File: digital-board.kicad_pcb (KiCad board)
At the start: 2 copper layers, 200 x 150 mm, 233 parts, among them IC1 ATMEGA6450-A, J1 CONN_20X2, Q1 2N3904, Q2 2N3904, SW15 TACT_SWITCH, SW16 TACT_SWITCH, SW17 TACT_SWITCH, SW18 TACT_SWITCH, SW19 TACT_SWITCH, SW20 TACT_SWITCH, SW21 TACT_SWITCH, SW22 TACT_SWITCH, SW23 TACT_SWITCH, U1 DG419, U10 74LVC1G32, U11 74HC165, U12 74AC595, U13 74AC595, U14 74HC165, U15 74AC595, U16 74AC595, U2 74HC4067, U3 R-78E5.0-1.0, U4 74HC4067, U5 74LS573, U6 74LS573, U7 74LVC2G04, U8 74AC595, U9 74HC165, X1 MIDI OUT, X2 MIDI IN, X3 MIDI THRU

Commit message: routing
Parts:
- removed C18: 0.1µ, synth:SM0603-JRL
- removed U11: 74HC165, github-smd:TSSOP-16
- moved R53 69.2 mm to (46.0, 51.0)
- moved C9 4.53 mm to (131.0, 72.0), turned to 270 degrees
- moved C17 3.04 mm to (187.0, 113.5), turned to 270 degrees
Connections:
- IC1 pad 86: Net-(IC1-Pad86) -> ~POTMUX EN0
- IC1 pad 87: Net-(IC1-Pad87) -> ~POTMUX EN1
- IC1 pad 90: ~POTMUX EN1 -> ISW10
- IC1 pad 91: ~POTMUX EN0 -> SW21
- IC1 pad 92: DGATE -> SW22
- IC1 pad 93: Net-(IC1-Pad93) -> ISW11
- IC1 pad 94: Net-(IC1-Pad94) -> ISW9
- IC1 pad 95: Net-(IC1-Pad95) -> ISW8
- IC1 pad 96: Net-(IC1-Pad96) -> DGATE
- ISW10 pad 2: Net-(ISW10-Pad2) -> ISW10
- ISW11 pad 2: Net-(ISW11-Pad2) -> ISW11
- ISW8 pad 2: Net-(ISW8-Pad2) -> ISW8
- ISW9 pad 2: Net-(ISW9-Pad2) -> ISW9
- R37 pad 2: Net-(ISW9-Pad2) -> ISW9
- R41 pad 2: Net-(ISW8-Pad2) -> ISW8
- R45 pad 2: Net-(R45-Pad2) -> SW21
- R51 pad 2: Net-(R51-Pad2) -> SW22
- R56 pad 2: Net-(ISW11-Pad2) -> ISW11
- R60 pad 2: Net-(ISW10-Pad2) -> ISW10
- SW21 pad 2: Net-(R45-Pad2) -> SW21
- SW22 pad 2: Net-(R51-Pad2) -> SW22
- U14 pad 15: GND -> ~SPI_EN
- U14 pad 9: Net-(U11-Pad10) -> SPI_MISO
- VR16 pad 2: Net-(U4-Pad6) -> Net-(U4-Pad8)
- VR17 pad 2: Net-(U4-Pad7) -> Net-(U4-Pad6)
- VR18 pad 2: Net-(U4-Pad8) -> Net-(U4-Pad7)
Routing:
- net ISW9: track 0.00 -> 140.6 mm, vias 0 -> 1
- net GND: track 3.57 -> 123.3 mm
- net DGATE: track 0.00 -> 104.0 mm, vias 0 -> 1
- net ISW8: track 0.00 -> 83.0 mm, vias 0 -> 1
- net ISW10: track 0.00 -> 82.7 mm, vias 0 -> 1
- net Net-(U4-Pad6): track 0.00 -> 77.0 mm
- net ISW11: track 0.00 -> 71.3 mm, vias 0 -> 1
- net SW22: track 0.00 -> 51.6 mm, vias 0 -> 1
- net SW21: track 0.00 -> 31.5 mm, vias 0 -> 1
- net Net-(ISW8-Pad2): track 26.8 -> 0.00 mm
- net Net-(U4-Pad7): track 76.5 -> 53.9 mm
- net Net-(U4-Pad8): track 53.3 -> 35.0 mm
- net Net-(ISW9-Pad2): track 11.3 -> 0.00 mm
- net Net-(R51-Pad2): track 10.8 -> 0.00 mm
- net Net-(R45-Pad2): track 10.8 -> 0.00 mm
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
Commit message: just before first ses import
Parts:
- R1: moved to F.Cu
- moved LED1 18.7 mm to (103.5, 164.0)
- moved R4 18.7 mm to (103.5, 162.0)
- moved R1 4.03 mm to (100.0, 140.5), turned to 0 degrees
- moved C5 4.00 mm to (114.0, 145.5), turned to 0 degrees
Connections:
- R4 pad 2: Net-(IC1-Pad4) -> Net-(R4-Pad2)
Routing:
- net +5V: track 347.2 -> 597.0 mm, vias 2 -> 1
- net UART TX: track 0.00 -> 245.5 mm
- net TUNE SEL: track 0.00 -> 167.4 mm, vias 0 -> 2
- net GATE: track 15.4 -> 130.7 mm, vias 0 -> 1
- net DISP CATHODE LATCH: track 0.00 -> 35.8 mm, vias 0 -> 2
- net DISP ANODE LATCH: track 0.00 -> 32.5 mm, vias 0 -> 2
- net ~RESET: track 17.9 -> 34.6 mm, vias 0 -> 1
- net Net-(IC1-Pad4): track 4.20 -> 0.00 mm
- net Net-(C3-Pad2): track 12.4 -> 15.9 mm
- net MISO: track 28.0 -> 31.3 mm
- net Net-(ISW11-Pad6): track 0.00 -> 2.95 mm
- net ISW10: track 82.7 -> 80.2 mm
- net Net-(LED1-Pad1): track 2.08 -> 0.00 mm
- net Net-(C5-Pad1): track 5.10 -> 6.79 mm
- net Net-(R42-Pad2): track 0.00 -> 1.63 mm, vias 0 -> 1
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
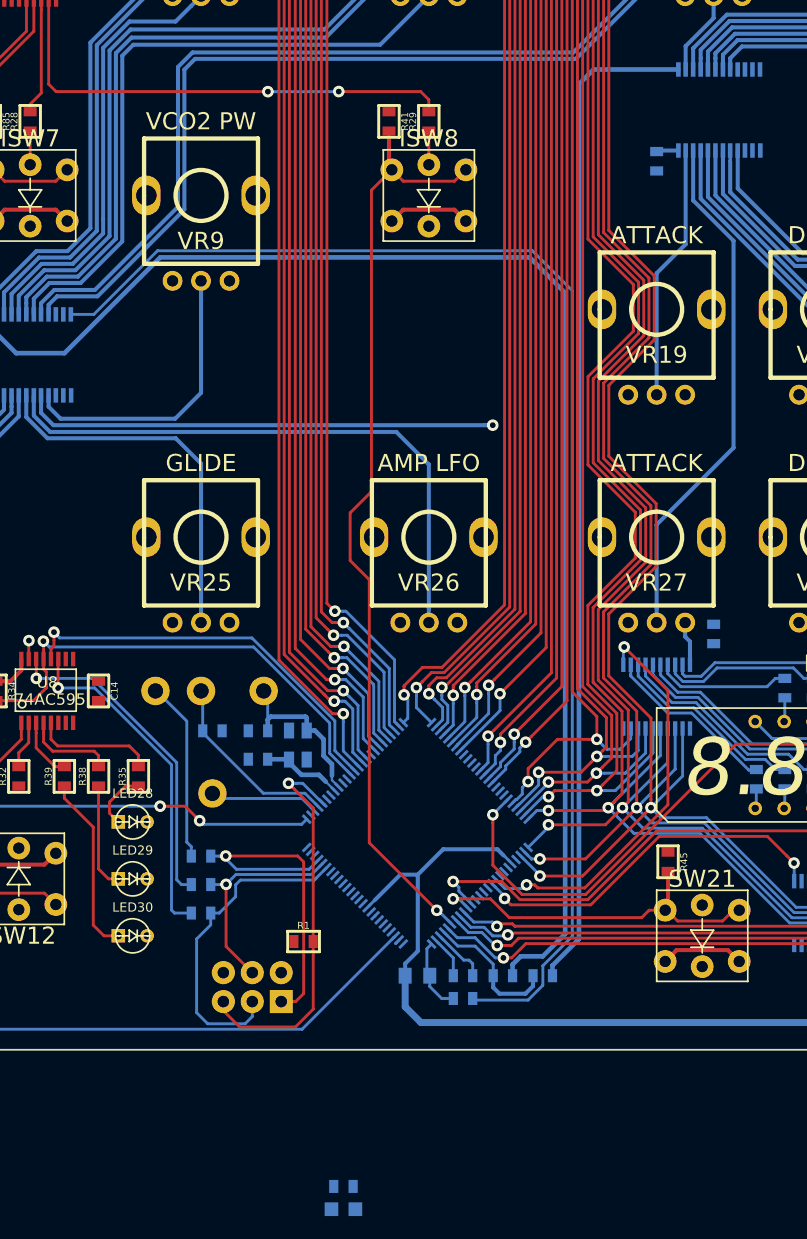
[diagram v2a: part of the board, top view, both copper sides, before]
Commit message: autorouter almost done - just need to fix short complete traces to MCU
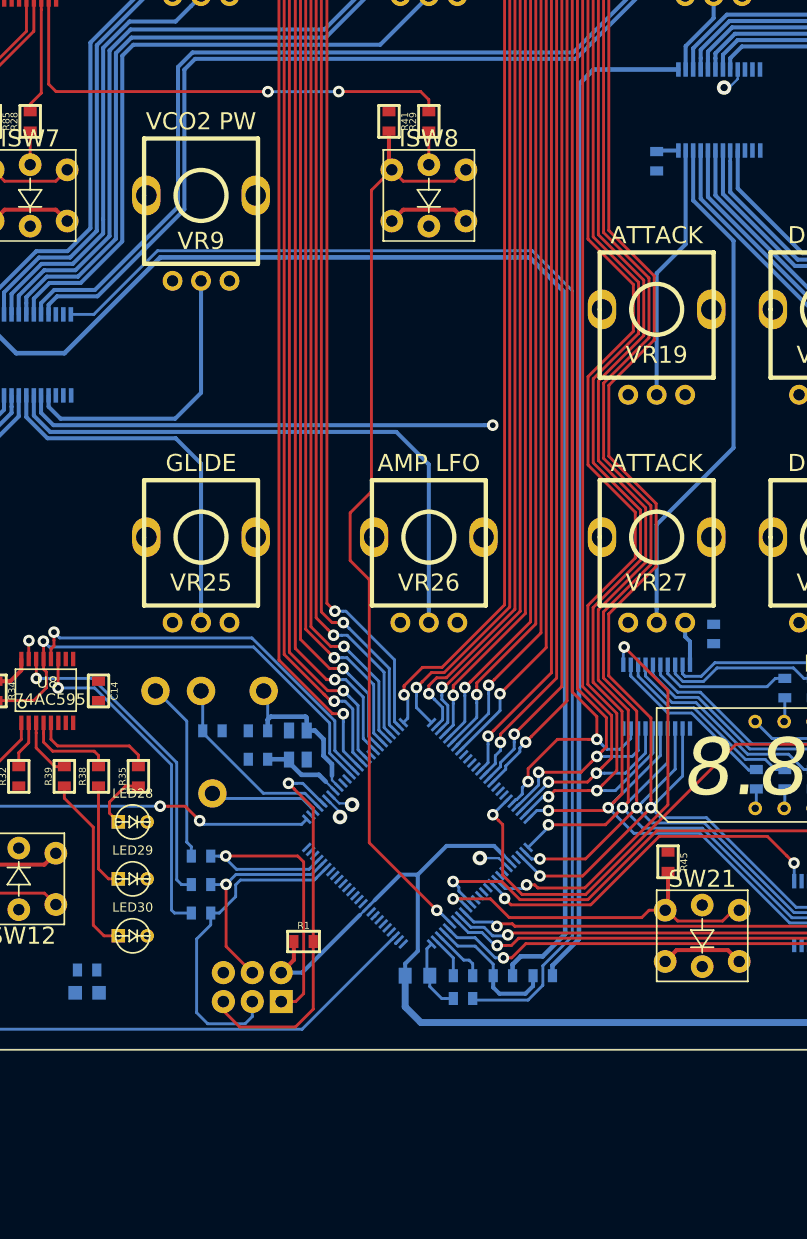
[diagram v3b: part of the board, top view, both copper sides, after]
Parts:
- moved LED1 29.4 mm to (81.0, 145.0)
- moved R4 29.4 mm to (81.0, 143.0)
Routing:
- net +5V: track 597.0 -> 612.4 mm, vias 1 -> 2
- net GND: track 122.3 -> 129.6 mm, vias 1 -> 4

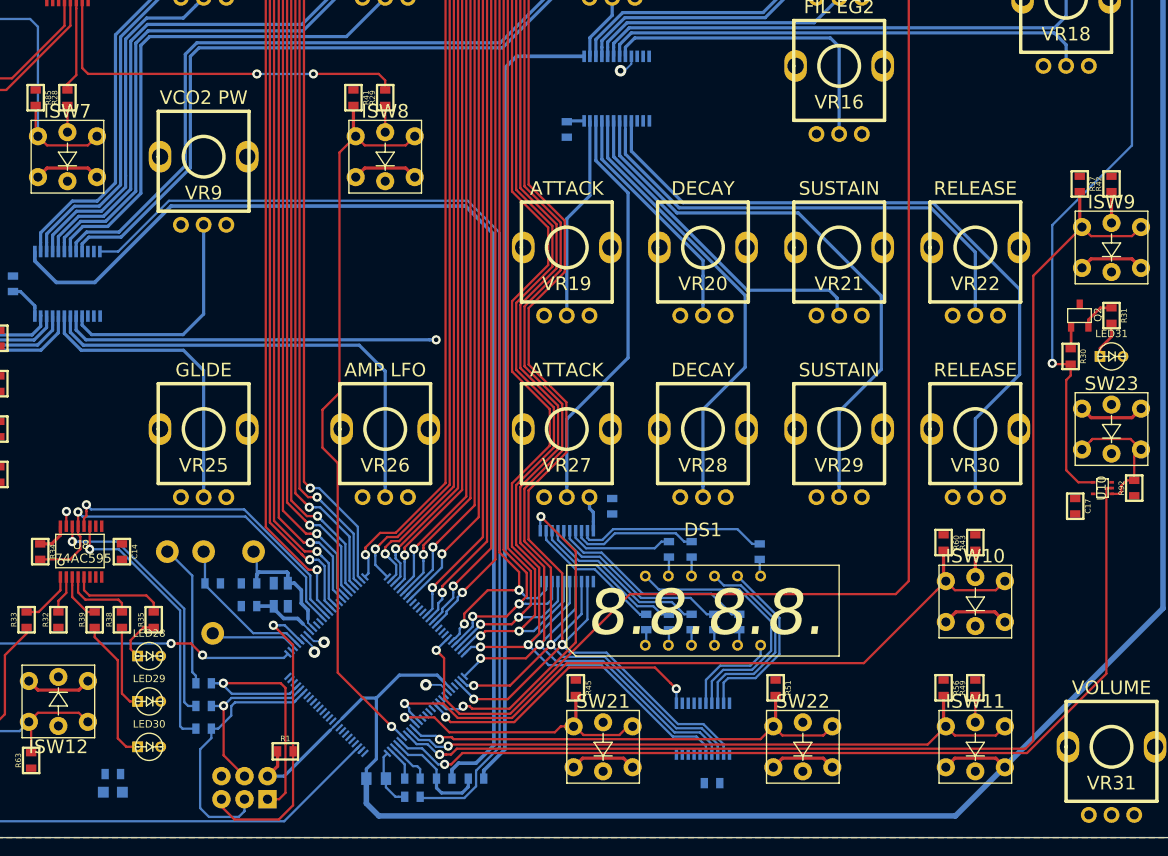
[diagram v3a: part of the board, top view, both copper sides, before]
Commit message: more routing before autorouting. can't fix short trace incompletes on MCU pins
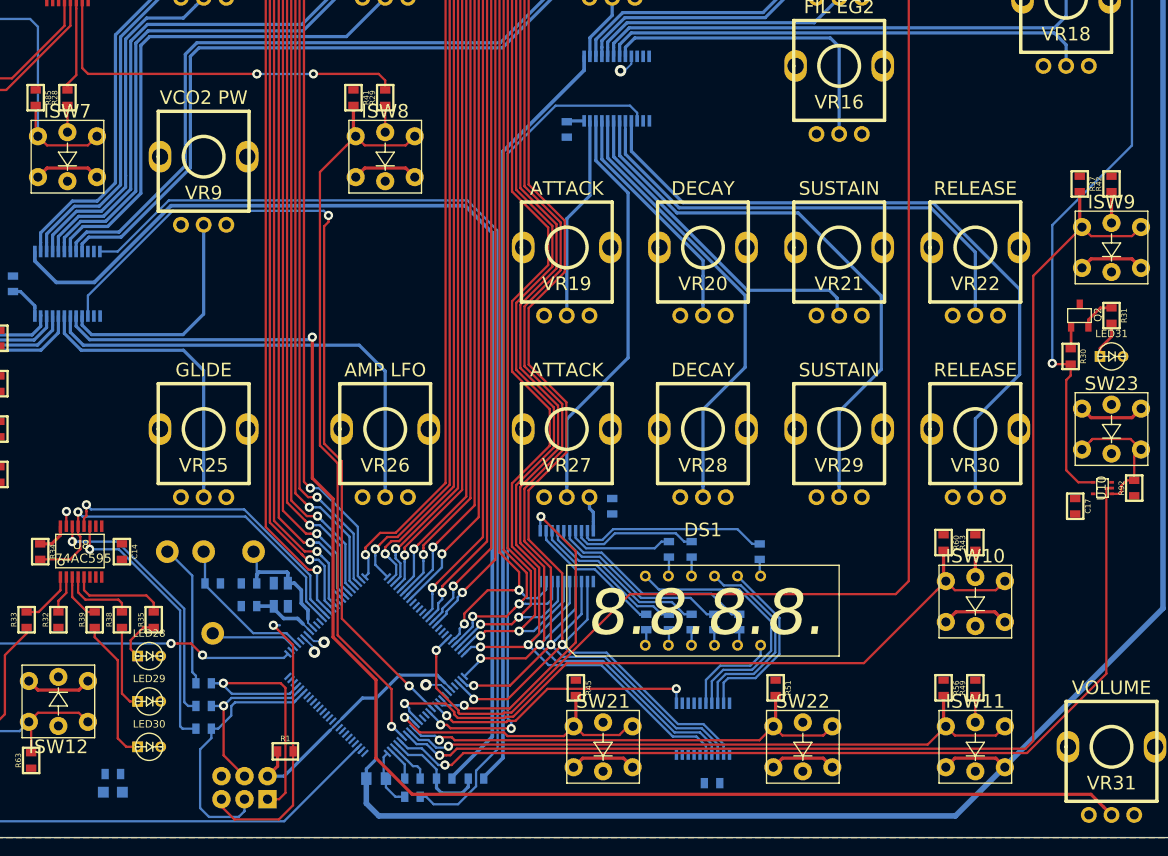
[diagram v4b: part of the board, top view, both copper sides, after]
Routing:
- net Net-(U2-Pad17): track 41.6 -> 160.8 mm
- net ~POTMUX EN0: track 0.00 -> 92.3 mm, vias 0 -> 2
- net ~POTMUX EN1: track 0.00 -> 91.1 mm, vias 0 -> 2
- net Net-(R6-Pad1): track 88.5 -> 84.1 mm
- net ~RESET: track 34.6 -> 31.4 mm
- net DISP ANODE LATCH: track 32.5 -> 30.4 mm
- net Net-(R3-Pad1): track 120.5 -> 119.1 mm

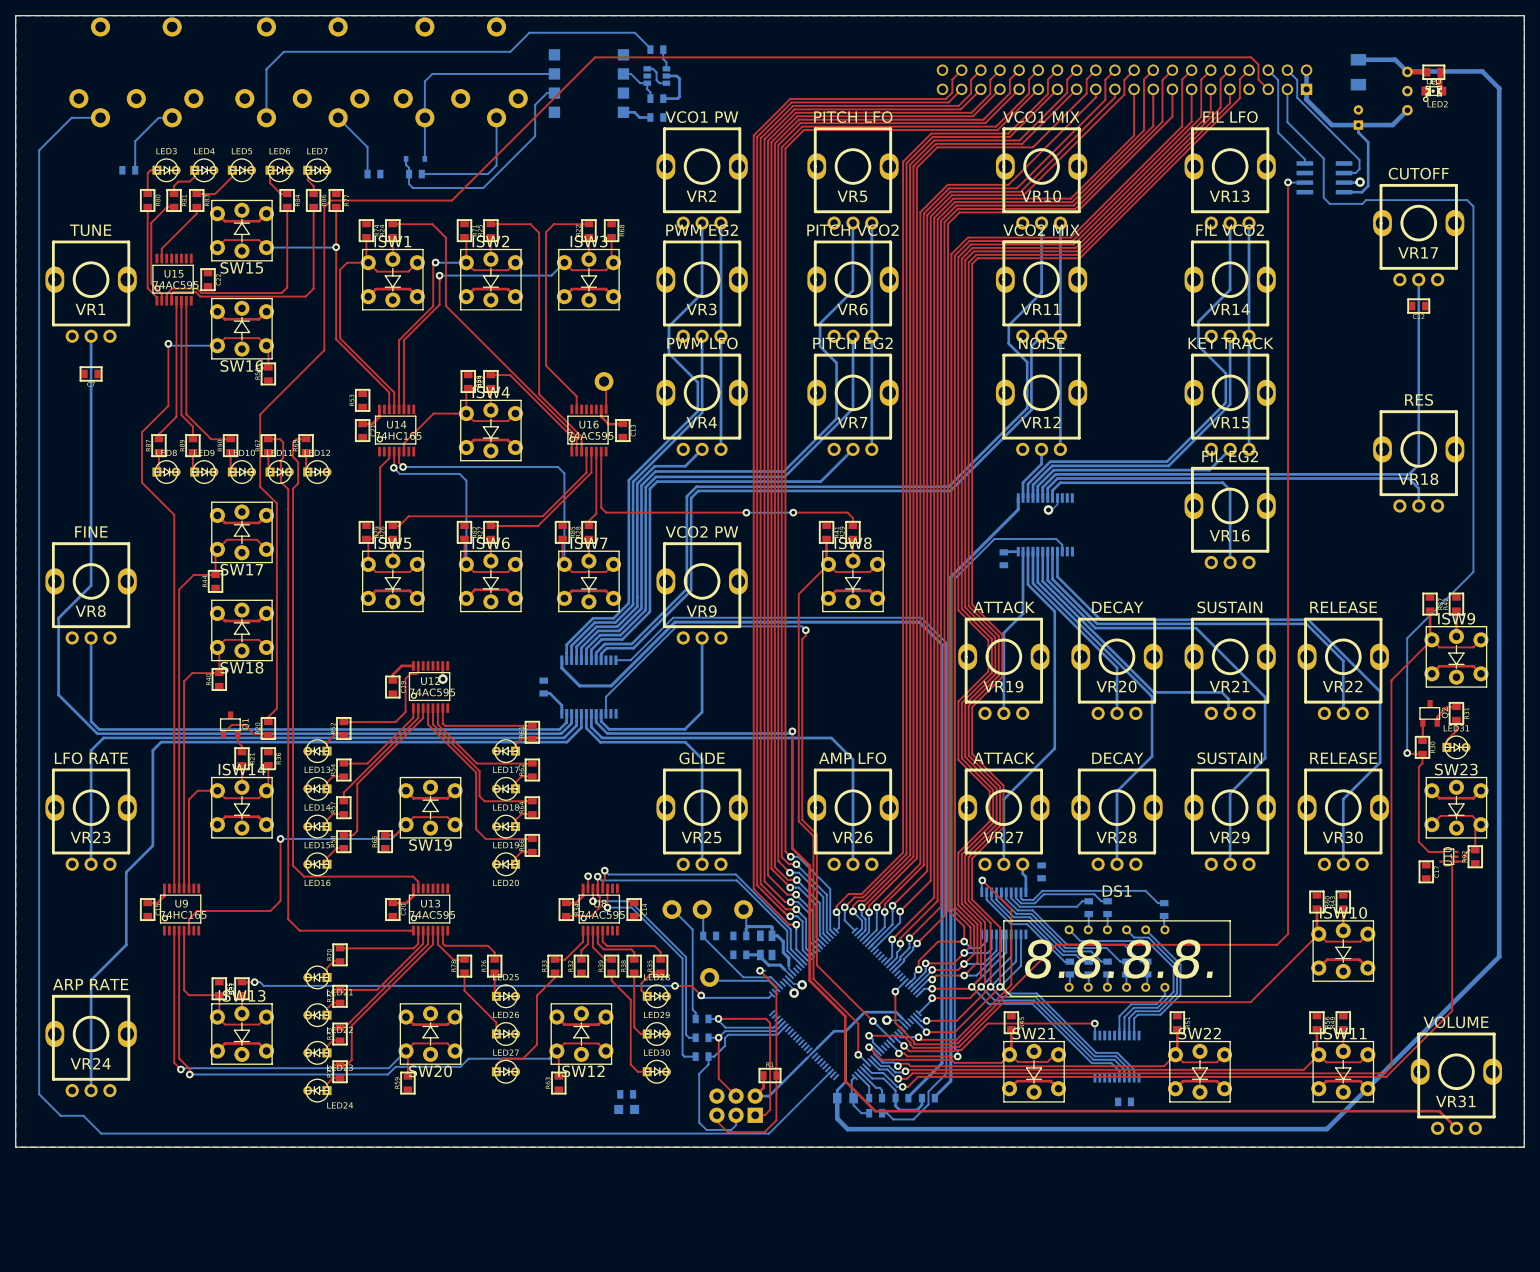
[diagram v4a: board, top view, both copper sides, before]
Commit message: more manual routing before autoroute
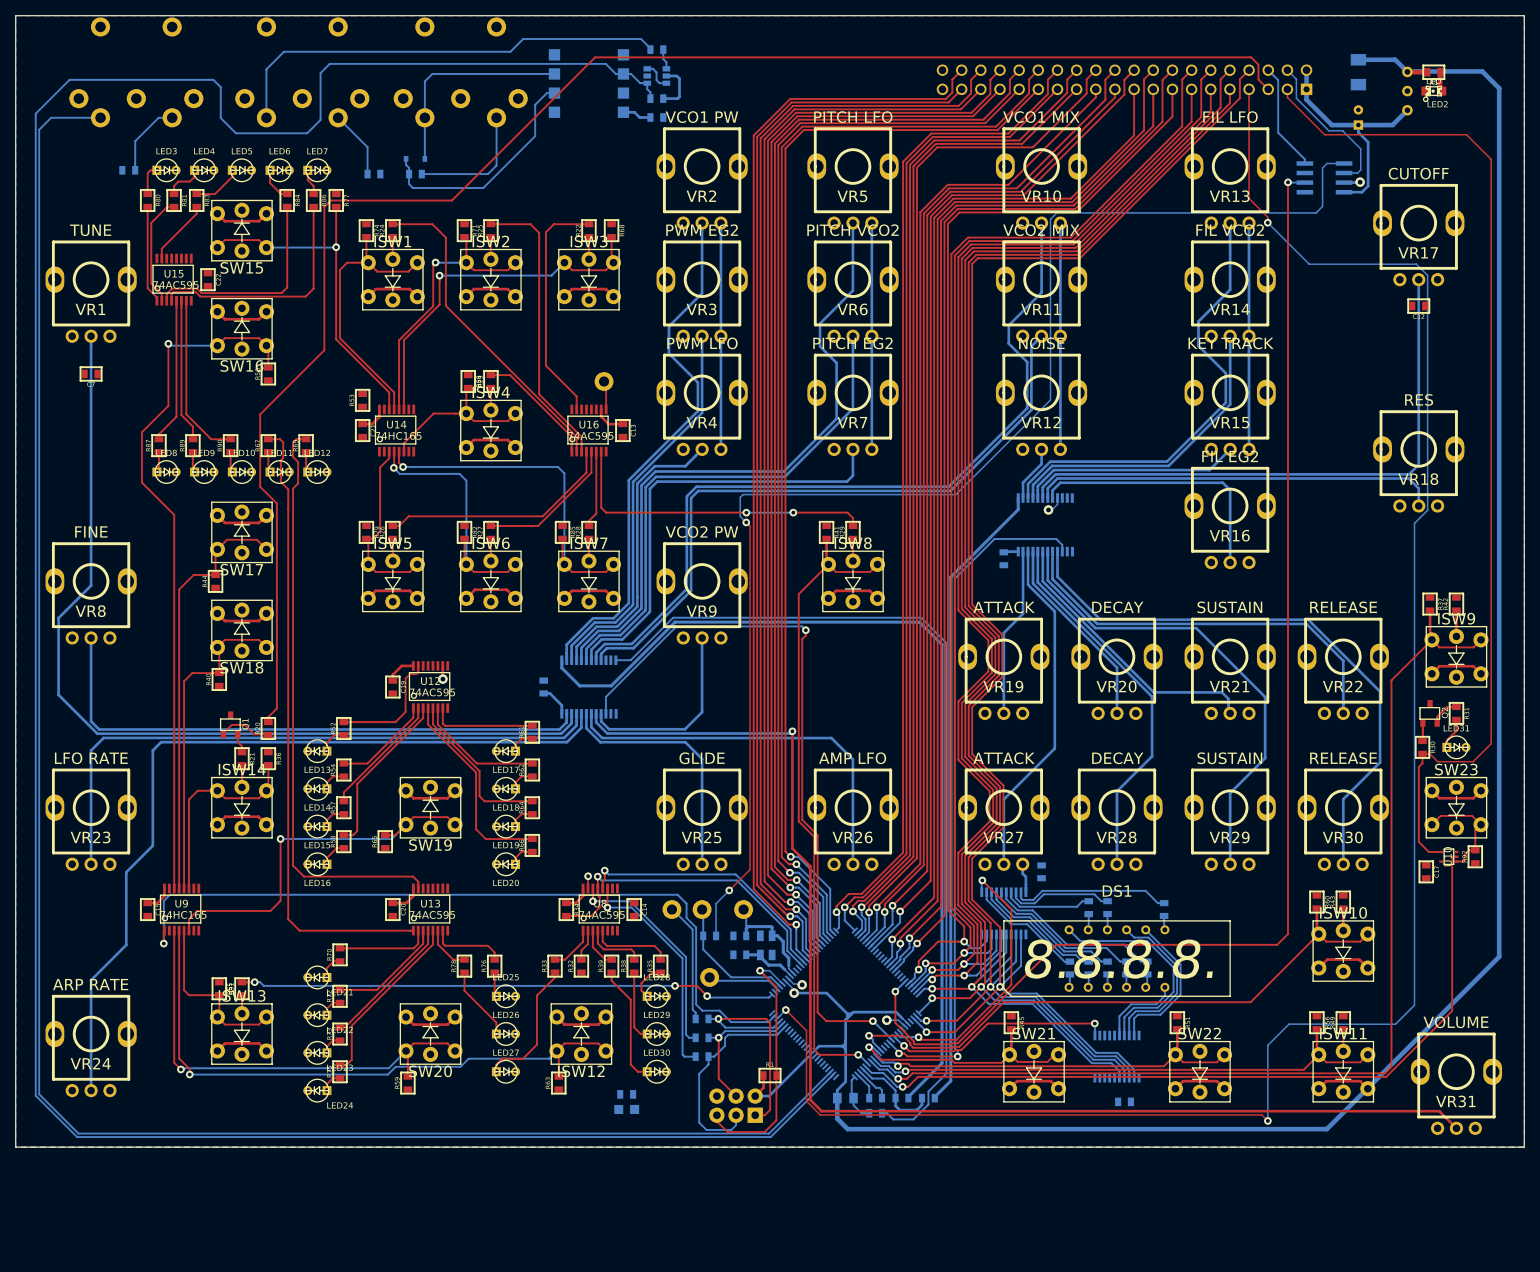
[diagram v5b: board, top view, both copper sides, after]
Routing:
- net UART RX: track 6.34 -> 341.1 mm
- net LFO RESET: track 0.00 -> 249.0 mm, vias 0 -> 3
- net Net-(R2-Pad2): track 0.00 -> 175.9 mm, vias 0 -> 2
- net SWITCH_LATCH: track 0.00 -> 103.3 mm, vias 0 -> 1
- net +5V: track 612.7 -> 623.9 mm
- net GATE: track 130.7 -> 134.9 mm, vias 1 -> 0
- net Net-(U2-Pad17): track 160.8 -> 164.9 mm
- net ~POTMUX EN0: track 92.3 -> 95.9 mm
- net ISW8: track 83.2 -> 86.2 mm
- net ~RESET: track 31.4 -> 34.4 mm
- net Net-(U2-Pad7): track 56.6 -> 58.6 mm
- net UART TX: track 245.5 -> 247.1 mm
- net TUNE: track 19.3 -> 20.7 mm
- net FREQ IN: track 16.6 -> 17.6 mm
- net Net-(R13-Pad1): track 60.4 -> 59.7 mm

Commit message: manual routing before autoroute
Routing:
- net Net-(R42-Pad2): track 1.63 -> 211.1 mm, vias 1 -> 2
- net Net-(R43-Pad2): track 0.00 -> 150.7 mm, vias 0 -> 2
- net LFO RESET: track 249.0 -> 216.0 mm
- net TUNE SEL: track 167.4 -> 170.9 mm
- net Net-(U2-Pad7): track 58.6 -> 56.6 mm
- net ISW9: track 140.8 -> 142.8 mm
- net Net-(R2-Pad2): track 175.9 -> 177.7 mm
- net Net-(U2-Pad8): track 106.1 -> 104.9 mm
- net /DAC10: track 130.3 -> 131.2 mm
- net ISW10: track 80.3 -> 81.2 mm
